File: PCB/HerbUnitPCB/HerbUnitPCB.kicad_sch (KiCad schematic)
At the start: 0 parts

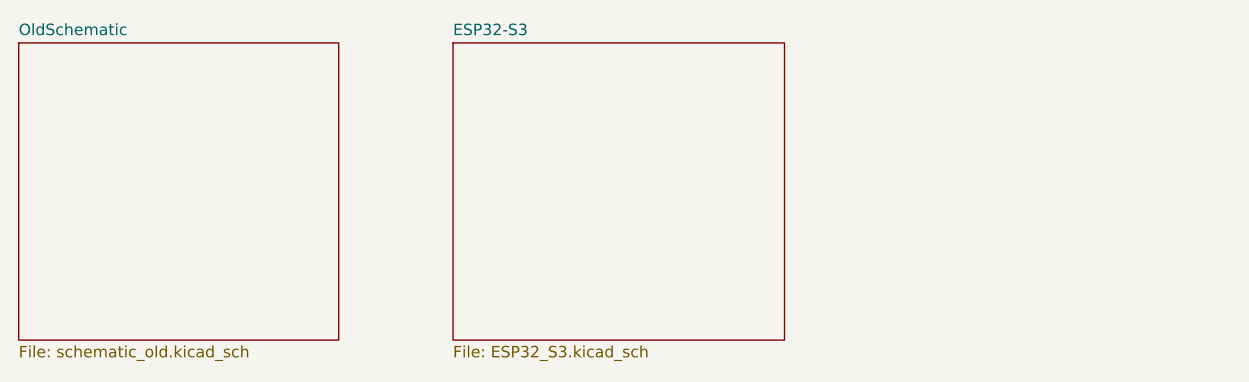
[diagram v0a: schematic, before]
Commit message: Schematic Progress
- Finished ESP Schematic
- Began Peripherals Schematic
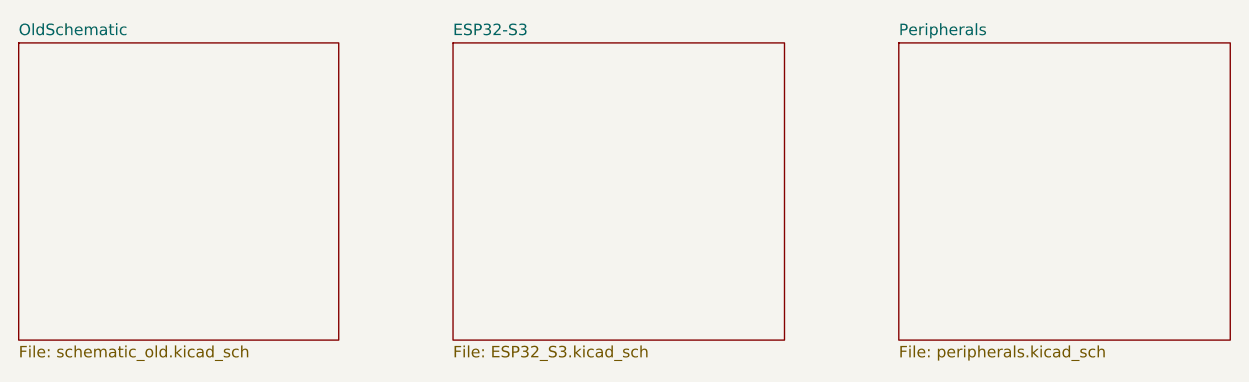
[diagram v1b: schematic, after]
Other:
- added sheet Peripherals (peripherals.kicad_sch)
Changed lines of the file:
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@@
 	(paper "A4")
+	(sheet
+		(at 134.62 68.58)
+		(size 36.83 33.02)
+		(exclude_from_sim no)
+		(in_bom yes)
+		(on_board yes)
+		(dnp no)
+		(fields_autoplaced yes)
+		(stroke
+			(width 0.1524)
+			(type solid)
+		)
+		(fill
+			(color 0 0 0 0)
+		)
+		(property "Sheetname" "Peripherals"
+			(at 134.62 67.8684 0)
+			(show_name no)
+			(do_not_autoplace no)
+			(effects
+				(font
+					(size 1.27 1.27)
+				)
+				(justify left bottom)
+			)
+		)
+		(property "Sheetfile" "peripherals.kicad_sch"
+			(at 134.62 102.1846 0)
+			(show_name no)
+			(do_not_autoplace no)
+			(effects
+				(font
+					(size 1.27 1.27)
+				)
+				(justify left top)
+			)
+		)
+		(instances
+			(project "HerbUnitPCB"
+				(path "/65cebcdd-0dc1-4eaa-a413-d7a78528268c"
+					(page "4")
+				)
+			)
+		)
+	)
 	(sheet
 		(at 36.83 68.58)
